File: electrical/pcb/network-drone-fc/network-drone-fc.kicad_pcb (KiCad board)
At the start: 4 copper layers, 36 x 39 mm, 94 parts, among them J1 U.FL-R-SMT-1, J2 TYPE-C 16PIN 2MD, J3 U.FL GPS, J4 ESC, J5 I2C port, J7 Charging board, U1 ESP32-S3FN8, U2 USBLC6-2SC6, U3 AP63205WU-7, U4 TLV75733PDBVR, U5 TPS7A2033PDBVR, U6 ICM-42688-P, U7 BMP581, U8 MAX-M10S, X1 Q22FA12800101

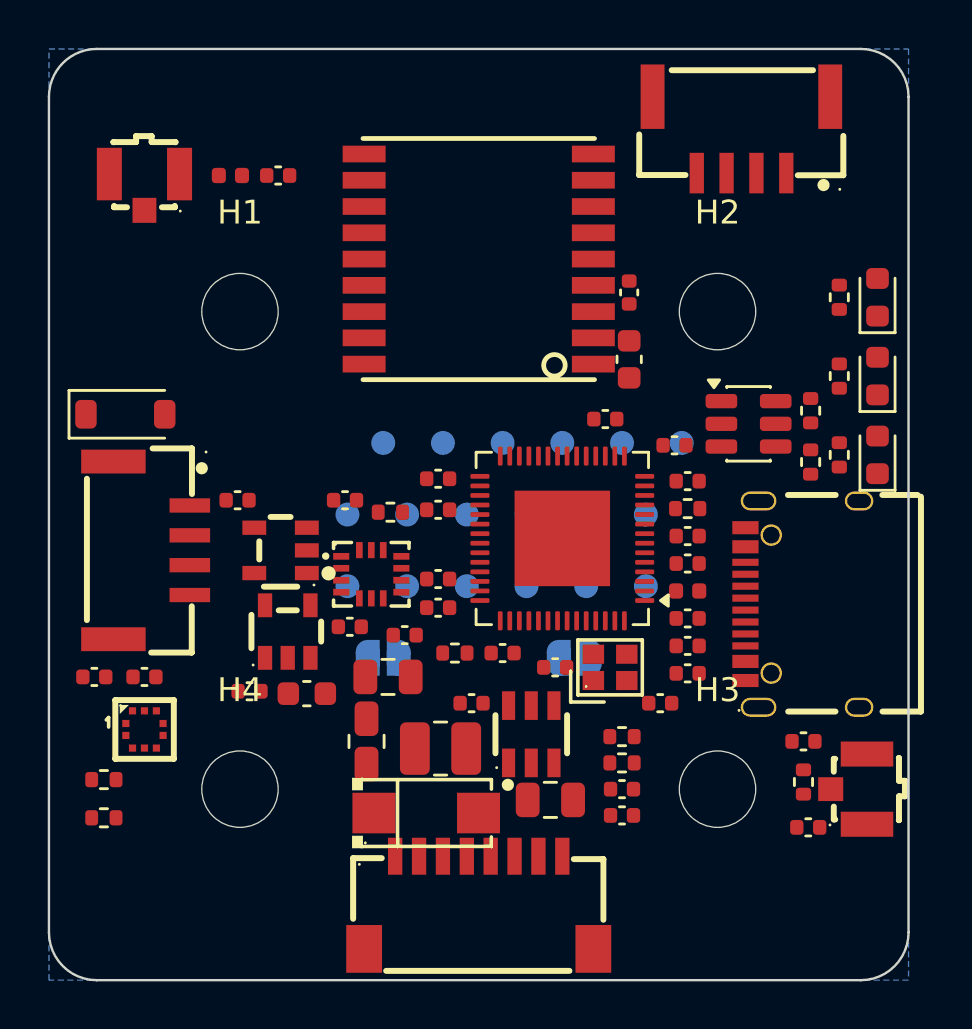
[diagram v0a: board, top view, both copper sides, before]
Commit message: PCB: placement reworked for routing; antenna, GPS feed, crystal, USB and buck routed by hand
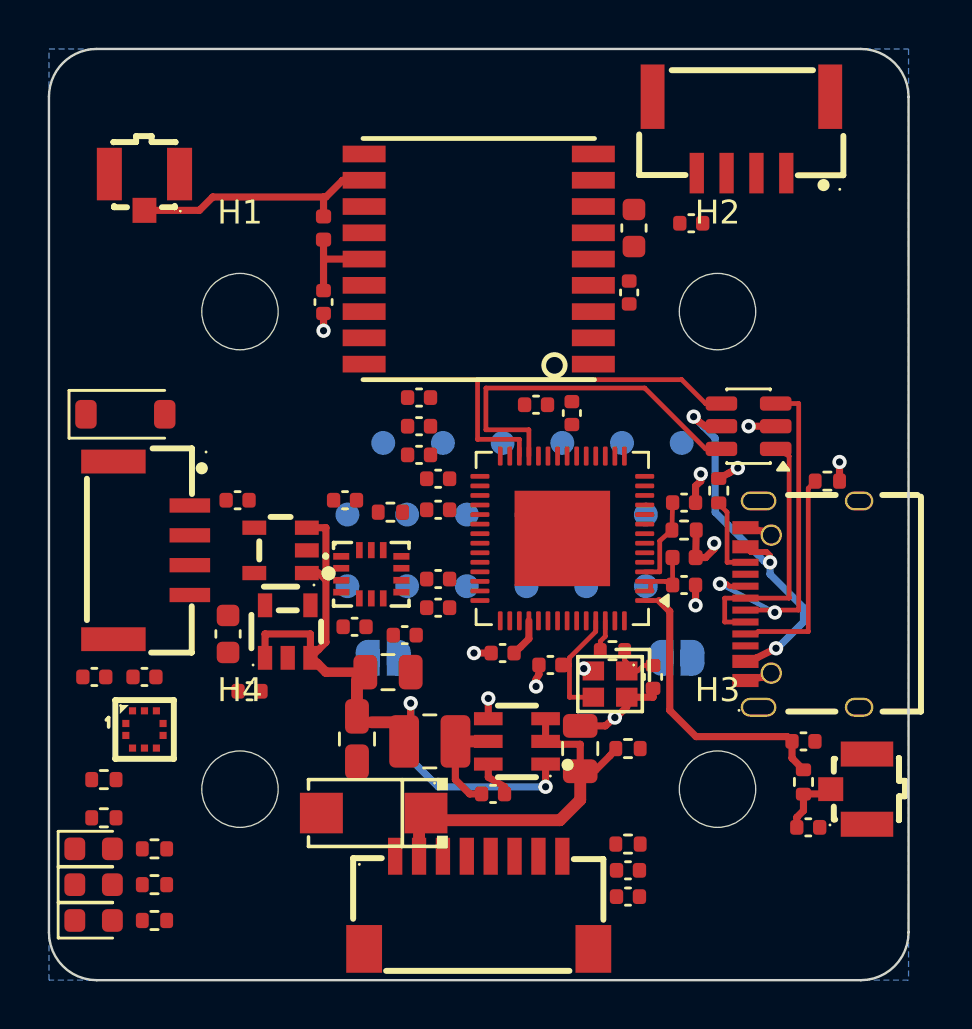
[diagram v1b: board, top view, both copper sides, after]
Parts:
- moved D2 40.1 mm to (83.9, 112.5), turned to 0 degrees
- moved D3 39.1 mm to (83.9, 114.0), turned to 0 degrees
- moved D4 38.2 mm to (83.9, 115.5), turned to 0 degrees
- moved R6 36.8 mm to (86.4, 112.5), turned to 0 degrees
- moved R7 35.7 mm to (86.4, 114.0), turned to 0 degrees
- moved R8 34.7 mm to (86.4, 115.5), turned to 0 degrees
- moved C6 16.1 mm to (97.5, 93.6)
- moved C3 12.2 mm to (97.5, 94.8)
- moved C2 12.1 mm to (97.5, 96.0)
- moved C5 11.9 mm to (102.4, 93.9)
- moved C34 9.33 mm to (108.9, 86.3)
- moved R2 6.60 mm to (105.6, 104.2)
- moved C32 5.63 mm to (93.5, 89.6), turned to -90 degrees
- moved C30 5.50 mm to (106.5, 86.5), turned to -90 degrees
- moved R4 5.10 mm to (110.0, 97.5)
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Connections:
- U2 pad 1: D+ -> D-
- U2 pad 3: D- -> D+
- U2 pad 4: USB_DN -> USB_DP
- U2 pad 6: USB_DP -> USB_DN
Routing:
- net +5V: track 0.00 -> 25.9 mm, vias 0 -> 2
- net VBUS: track 0.00 -> 16.4 mm, vias 0 -> 3
- net D+: track 0.00 -> 15.6 mm, vias 0 -> 2
- net USB_DP: track 0.00 -> 15.6 mm
- net USB_DN: track 0.00 -> 15.6 mm
- net VBAT: track 0.00 -> 15.2 mm
- net GND: track 0.00 -> 15.0 mm, vias 0 -> 11
- net Antenna: track 0.00 -> 12.4 mm
- net D-: track 0.00 -> 11.2 mm
- net Net-(J3-SIG): track 0.00 -> 10.5 mm
- net Net-(J2-CC1): track 0.00 -> 9.09 mm
- net XTAL_N: track 0.00 -> 4.98 mm
- net +3V3: track 0.00 -> 3.93 mm, vias 0 -> 1
- net Net-(U8-VCC_RF): track 0.00 -> 3.84 mm
- net Net-(JP1-B): track 0.00 -> 3.76 mm
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
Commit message: PCB: fully routed, GND and +3V3 planes, 160 vias, DRC clean
Antenna, GPS feed, crystal, USB, buck and IMU SPI by hand; the rest on a 0.1 mm grid router kept to two signal layers. In1 is solid GND, In2 is solid +3V3, top and bottom carry GND fills. Test pads sit on vias of their nets. DRC: 0 errors, 0 unconnected; only silkscreen warnings remain.
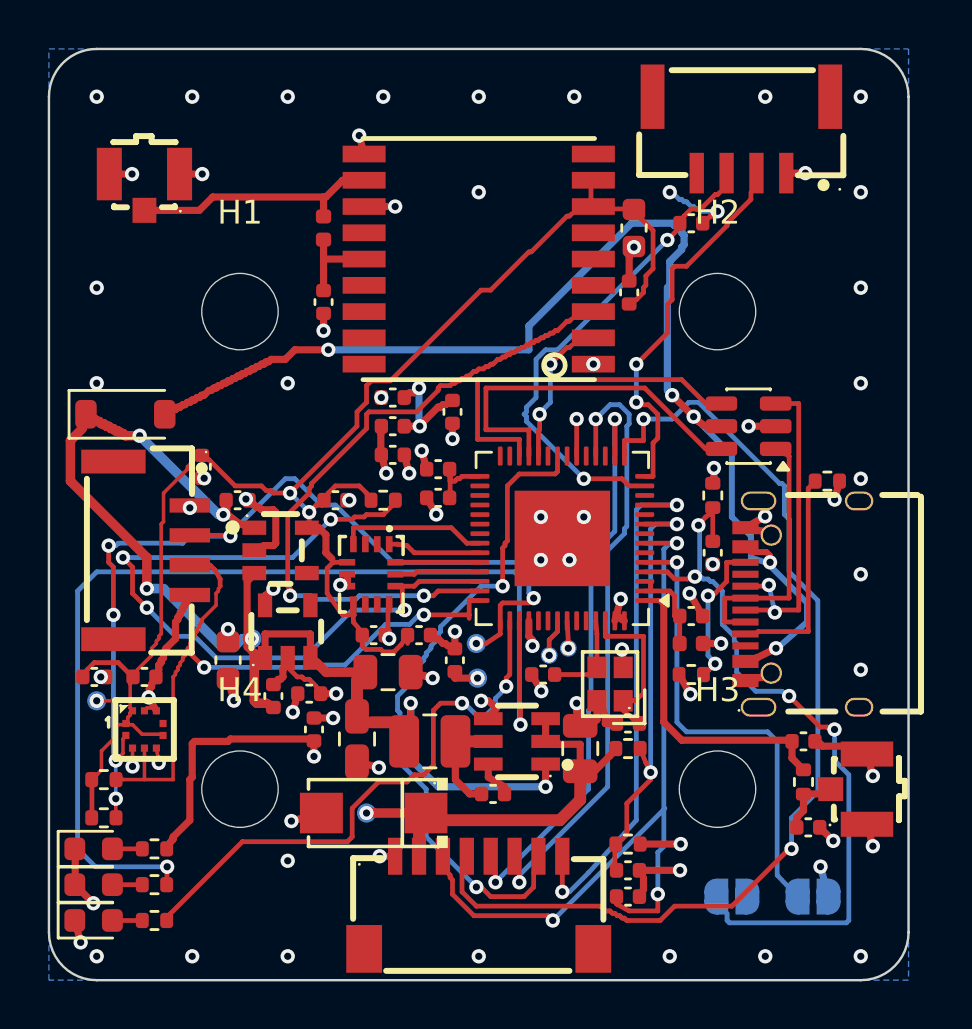
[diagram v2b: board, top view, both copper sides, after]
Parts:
- removed R2: 0, R_0402_1005Metric
- removed TP10, TP11, TP12, TP14, TP15, TP16, TP17, TP18, TP7, TP8, TP9: TestPoint, TestPoint:TestPoint_Pad_D1.0mm
- moved TP6 26.8 mm to (84.0, 106.3)
- moved JP1 17.7 mm to (110.6, 114.5)
- moved TP3 16.5 mm to (95.3, 111.0)
- moved C5 16.5 mm to (93.1, 107.5), turned to 90 degrees
- moved TP4 15.4 mm to (90.5, 103.7)
- moved TP5 11.6 mm to (100.0, 105.3)
- moved C26 11.5 mm to (88.4, 96.5), turned to 90 degrees
- moved JP2 11.5 mm to (114.0, 114.5)
- moved TP1 11.3 mm to (103.0, 104.4)
- moved TP2 10.1 mm to (103.8, 104.1)
- moved R4 7.79 mm to (108.9, 105.2), turned to 180 degrees
- moved TP13 5.91 mm to (99.9, 103.9)
- moved C7 5.00 mm to (98.9, 94.2)
- moved L1 3.61 mm to (108.9, 103.9)
- moved C25 3.58 mm to (95.6, 103.5)
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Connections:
- C12 pad 1: Net-(X1-OSC1) -> XTAL_P
- U1 pad 10: MOTOR2 -> (no net)
- U1 pad 11: MOTOR3 -> MOTOR4
- U1 pad 12: MOTOR4 -> (no net)
- U1 pad 14: ICM_INT2 -> DOCK_DET
- U1 pad 15: ICM_CS -> ESC_TELEM
- U1 pad 16: SPI_MOSI -> MOTOR1
- U1 pad 17: SPI_SCK -> (no net)
- U1 pad 18: SPI_MISO -> MOTOR2
- U1 pad 21: ICM_INTR -> (no net)
- U1 pad 22: (no net) -> MOTOR3
- U1 pad 23: ESC_TELEM -> (no net)
- U1 pad 24: DOCK_DET -> GPS_RX
- U1 pad 36: Yellow -> ICM_INTR
- U1 pad 37: Green -> SPI_MISO
- U1 pad 38: I2C_SDA -> SPI_MOSI
- U1 pad 39: I2C_SCL -> SPI_SCK
- U1 pad 40: GPS_TX -> ICM_CS
- U1 pad 41: GPS_RX -> GPS_TX
- U1 pad 42: UART_TX -> I2C_SDA
- U1 pad 43: UART_RX -> I2C_SCL
- U1 pad 44: (no net) -> Yellow
- U1 pad 45: (no net) -> Green
- U1 pad 6: VBAT_SENSE -> (no net)
- U1 pad 9: MOTOR1 -> VBAT_SENSE
- U6 pad 9: ICM_INT2 -> (no net)
- X1 pad 1: Net-(X1-OSC1) -> XTAL_P
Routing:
- net +3V3_SENS: track 0.00 -> 66.4 mm, vias 0 -> 3
- net GND: track 15.0 -> 68.6 mm, vias 11 -> 80
- net Green: track 0.00 -> 45.1 mm, vias 0 -> 2
- net ESC_TELEM: track 0.00 -> 42.6 mm, vias 0 -> 2
- net I2C_SCL: track 0.00 -> 39.1 mm, vias 0 -> 7
- net VBUS: track 16.4 -> 51.0 mm, vias 3 -> 5
- net ICM_CS: track 0.00 -> 32.0 mm, vias 0 -> 4
- net ESC_CUR: track 0.00 -> 31.7 mm, vias 0 -> 3
- net I2C_SDA: track 0.00 -> 28.8 mm, vias 0 -> 2
- net GPS_TX: track 0.00 -> 27.5 mm, vias 0 -> 2
- net Net-(JP1-B): track 3.76 -> 30.7 mm, vias 0 -> 4
- net MOTOR3: track 0.00 -> 26.6 mm, vias 0 -> 2
- net MOTOR2: track 0.00 -> 25.3 mm, vias 0 -> 2
- net Yellow: track 0.00 -> 23.8 mm, vias 0 -> 2
- net +5V: track 25.9 -> 49.5 mm, vias 2 -> 6
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- added copper zone on In2.Cu, net +3V3
- added copper zone on F.Cu, net GND

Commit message: PCB: straighten the router's staircase tracks (999 segments down to 544)
Each chain of grid steps is replaced by the fewest straight or 45 degree segments that still clear every other item. Same vias, same paths, DRC still 0 errors.
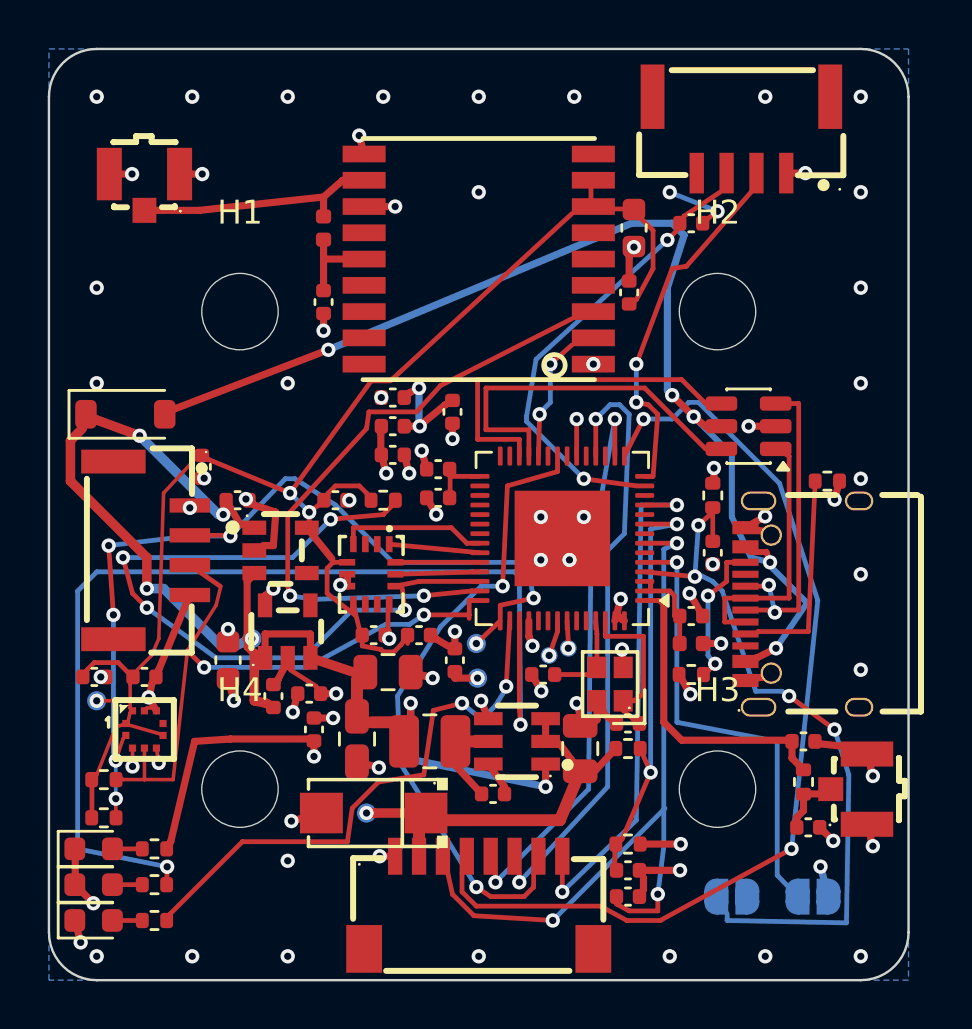
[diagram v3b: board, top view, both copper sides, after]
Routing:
- net VBUS: track 51.0 -> 48.0 mm
- net ESC_TELEM: track 42.6 -> 40.5 mm
- net +3V3_SENS: track 66.4 -> 64.4 mm
- net GND: track 68.6 -> 66.9 mm
- net I2C_SDA: track 28.8 -> 27.7 mm
- net Net-(JP1-B): track 30.7 -> 29.7 mm
- net MOTOR3: track 26.6 -> 25.6 mm
- net +5V: track 49.5 -> 48.6 mm
- net I2C_SCL: track 39.1 -> 38.2 mm
- net GPS_TX: track 27.5 -> 26.6 mm
- net VBAT: track 17.7 -> 17.0 mm
- net DOCK_DET: track 15.2 -> 14.6 mm
- net AUX_ADC: track 19.3 -> 18.7 mm
- net Yellow: track 23.8 -> 23.3 mm

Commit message: PCB: shorten Green, ICM_CS pull-up and GPS_TX (45, 31 and 27 mm down to 25, 10 and 20 mm)
Each net was ripped up and rerouted with everything else fixed in place and vias priced cheaply. The old Green run along the west edge had been walling off the CS pull-up. 158 vias, DRC 0 errors.
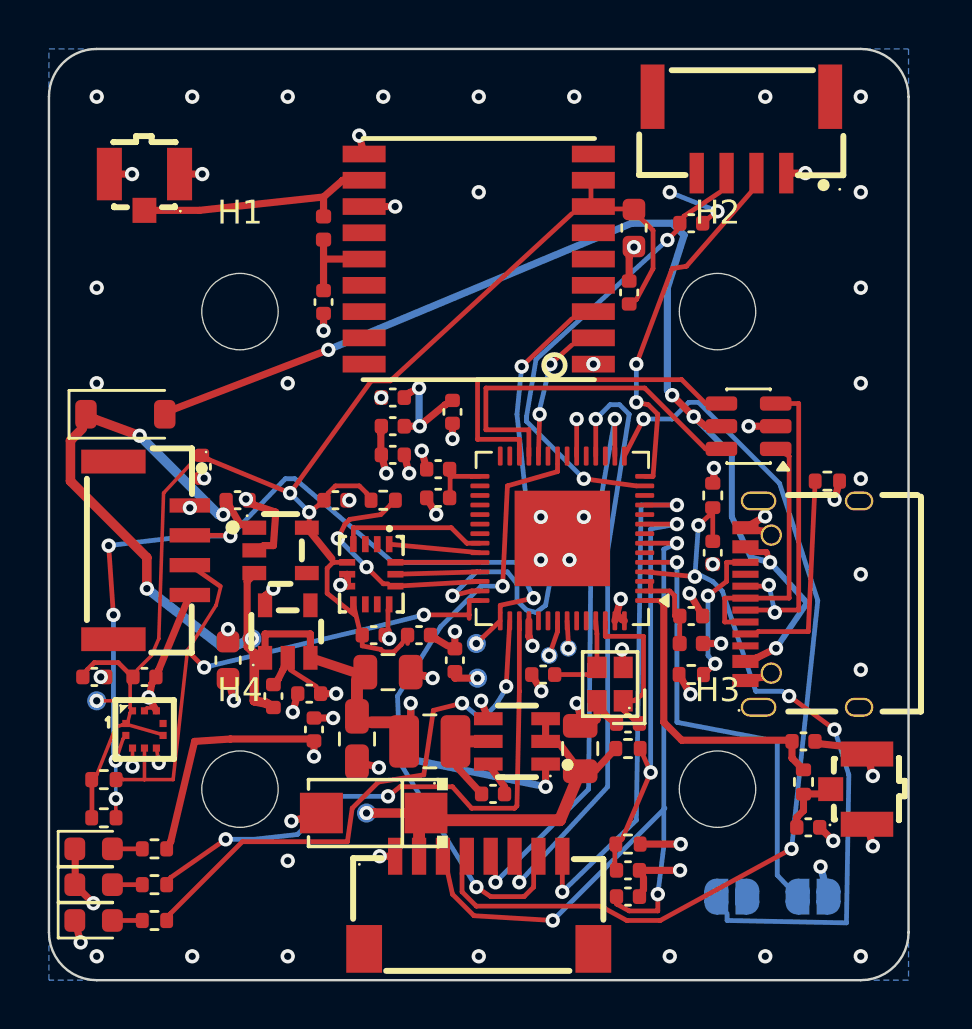
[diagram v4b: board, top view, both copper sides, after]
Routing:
- net ICM_CS: track 31.5 -> 9.56 mm, vias 4 -> 2
- net Green: track 44.8 -> 24.4 mm
- net GPS_TX: track 26.6 -> 20.1 mm

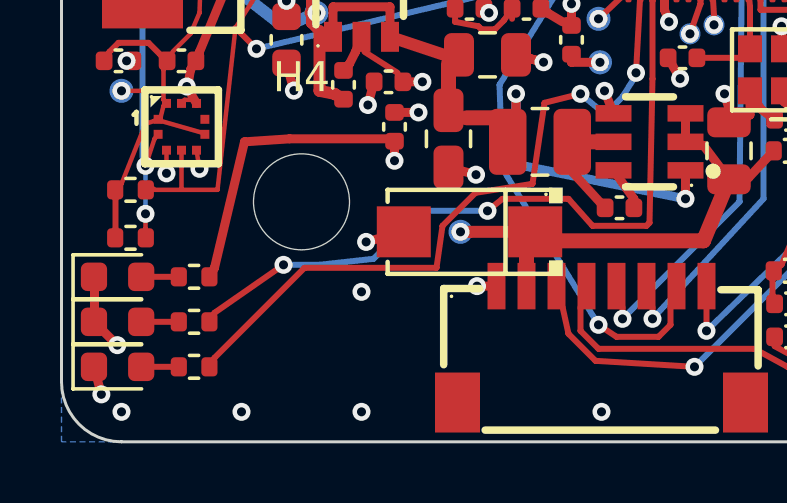
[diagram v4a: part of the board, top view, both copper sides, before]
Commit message: PCB: C35 on the bottom side at the lower-left corner, tied to the VBAT test-point via; DRC clean
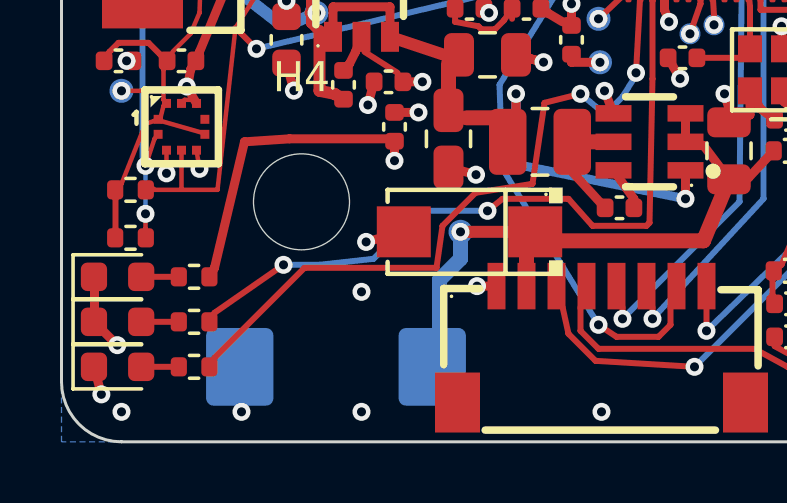
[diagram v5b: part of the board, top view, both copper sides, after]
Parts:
- added C35: 100uF 25V polymer, CP_EIA-7343-31_Kemet-D_HandSolder, B.Cu at (91.2, 115.5)
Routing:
- net VBAT: track 17.0 -> 21.4 mm
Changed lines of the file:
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@@
 		(embedded_fonts no)
 	)
+	(footprint "CP_EIA-7343-31_Kemet-D_HandSolder"
+		(layer "B.Cu")
+		(at 91.15 115.5 180)
+		(descr "Tantalum Capacitor SMD Kemet-D (7343-31 Metric), IPC-7352 nominal, (Body size from: http://www.kemet.com/Lists/ProductCatalog/Attachments/253/KEM_TC101_STD.pdf), generated with kicad-footprint-generator")
+		(tags "capacitor tantalum")
+		(property "Reference" "C35"
+			(at 0 3.1 0)
+			(layer "B.SilkS")
+			(effects
+				(font
+					(size 1 1)
+					(thickness 0.15)
+				)
+				(justify mirror)
+			)
+		)
+		(property "Value" "100uF 25V polymer"
+			(at 0 -3.1 0)
+			(layer "B.Fab")
+			(effects
+				(font
+					(size 1 1)
+					(thickness 0.15)
+				)
+				(justify mirror)
+			)
+		)
+		(property "Datasheet" ""
+			(at 0 0 0)
+			(layer "B.Fab")
+			(hide yes)
+			(effects
+				(font
+					(size 1.27 1.27)
+					(thickness 0.15)
+				)
+				(justify mirror)
+			)
+		)
+		(property "Description" ""
+			(at 0 0 0)
+			(layer "B.Fab")
+			(hide yes)
+			(effects
+				(font
+					(size 1.27 1.27)
+					(thickness 0.15)
+				)
+				(justify mirror)
+			)
+		)
+		(attr smd)
+		(fp_line
+			(start 3.65 2.26)
+			(end -4.59 2.26)
+			(stroke
+				(width 0.12)
+				(type solid)
+			)
+			(layer "B.SilkS")
+		)
+		(fp_line
+			(start -4.59 2.26)
+			(end -4.59 -2.26)
+			(stroke
+				(width 0.12)
+				(type solid)
+			)
+			(layer "B.SilkS")
+		)
+		(fp_line
+			(start -4.59 -2.26)
+			(end 3.65 -2.26)
+			(stroke
+				(width 0.12)
+				(type solid)
+			)
+			(layer "B.SilkS")
+		)
+		(fp_rect
+			(start -4.58 2.4)
+			(end 4.58 -2.4)
+			(stroke
+				(width 0.05)
+				(type solid)
+			)
+			(fill no)
+			(layer "B.CrtYd")
+		)
+		(fp_line
+			(start 3.65 2.15)
+			(end -2.65 2.15)
+			(stroke
+				(width 0.1)
+				(type solid)
+			)
+			(layer "B.Fab")
+		)
+		(fp_line
+			(start 3.65 -2.15)
+			(end 3.65 2.15)
+			(stroke
+				(width 0.1)
+				(type solid)
+			)
+			(layer "B.Fab")
+		)
+		(fp_line
+			(start -2.65 2.15)
+			(end -3.65 1.15)
+			(stroke
+				(width 0.1)
+				(type solid)
+			)
+			(layer "B.Fab")
+		)
+		(fp_line
+			(start -3.65 1.15)
+			(end -3.65 -2.15)
+			(stroke
+				(width 0.1)
+				(type solid)
+			)
+			(layer "B.Fab")
+		)
+		(fp_line
+			(start -3.65 -2.15)
+			(end 3.65 -2.15)
+			(stroke
+				(width 0.1)
+				(type solid)
+			)
+			(layer "B.Fab")
+		)
+		(fp_text user "${REFERENCE}"
+			(at 0 0 0)
+			(layer "B.Fab")
+			(effects
+				(font
+					(size 1 1)
+					(thickness 0.15)
+				)
+				(justify mirror)
+			)
+		)
+		(pad "1" smd roundrect
+			(at -3.2075 0 180)
+			(size 2.245 2.59)
+			(layers "B.Cu" "B.Mask" "B.Paste")
+			(roundrect_rratio 0.111359)
+			(net 43 "VBAT")
+		)
+		(pad "2" smd roundrect
+			(at 3.2075 0 180)
+			(size 2.245 2.59)
+			(layers "B.Cu" "B.Mask" "B.Paste")
+			(roundrect_rratio 0.111359)
+			(net 2 "GND")
+		)
+		(embedded_fonts no)
+		(model "${KICAD9_3DMODEL_DIR}/Capacitor_Tantalum_SMD.3dshapes/CP_EIA-7343-31_Kemet-D.step"
+			(offset
+				(xyz 0 0 0)
+			)
+			(scale
+				(xyz 1 1 1)
+			)
+			(rotate
+				(xyz 0 0 0)
+			)
+		)
+	)
 	(footprint "Jumper:SolderJumper-2_P1.3mm_Open_RoundedPad1.0x1.5mm"
 		(layer "B.Cu")
@@
 		(net 43)
 	)
+	(segment
+		(start 95.3 111)
+		(end 95.3 111.9)
+		(width 0.5)
+		(layer "B.Cu")
+		(net 43)
+	)
+	(segment
+		(start 94.6 112.6)
+		(end 94.6 115.1)
+		(width 0.5)
+		(layer "B.Cu")
+		(net 43)
+	)
+	(segment
+		(start 95.3 111.9)
+		(end 94.6 112.6)
+		(width 0.5)
+		(layer "B.Cu")
+		(net 43)
+	)
